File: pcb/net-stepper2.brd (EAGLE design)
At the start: 90.2 x 41.9 mm, 42 parts, among them J1 MICRO-USB, J2 POWER_JACKPTH_LOCK, J3 ENCODER, J4 ENDSTOP2, J5 ENDSTOP1, J6 STEPER, Q1 600mA/40V, Q2 600mA/40V, U1 L6470, U2 CP2104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

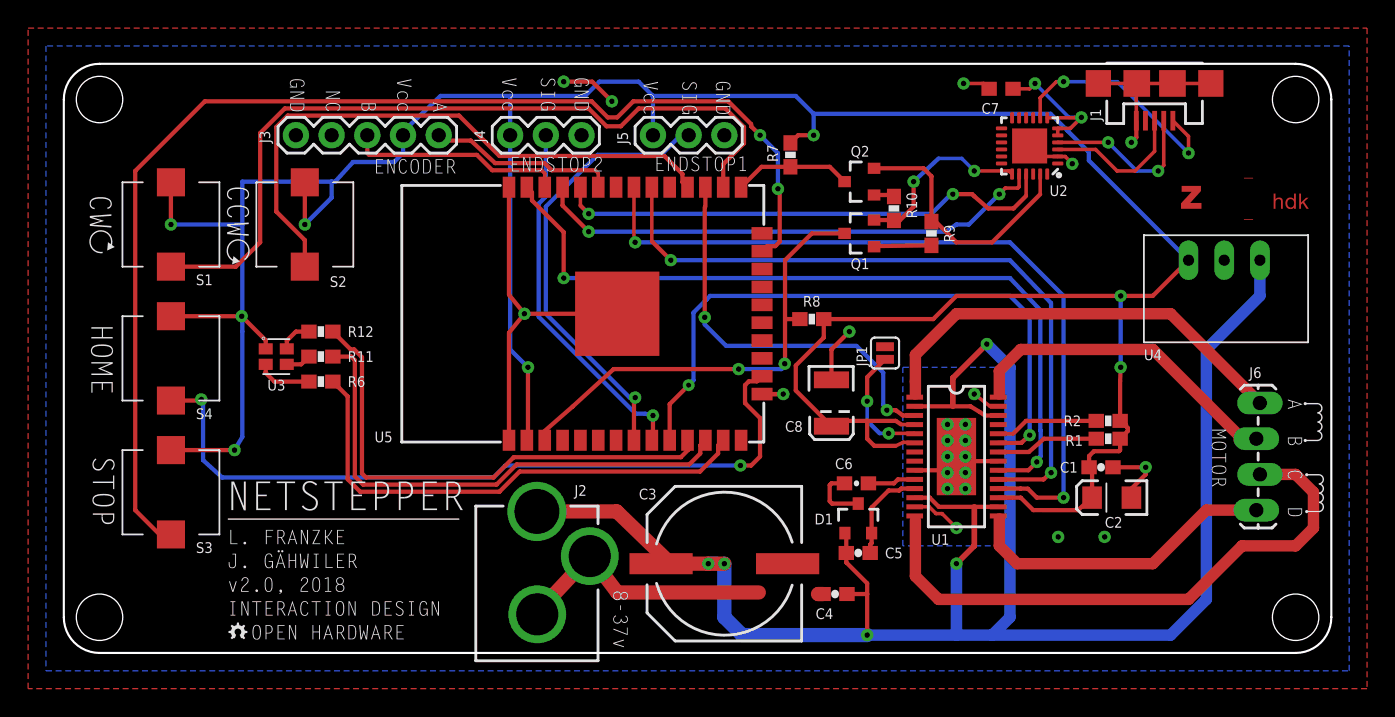
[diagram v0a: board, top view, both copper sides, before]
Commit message: Drill size change
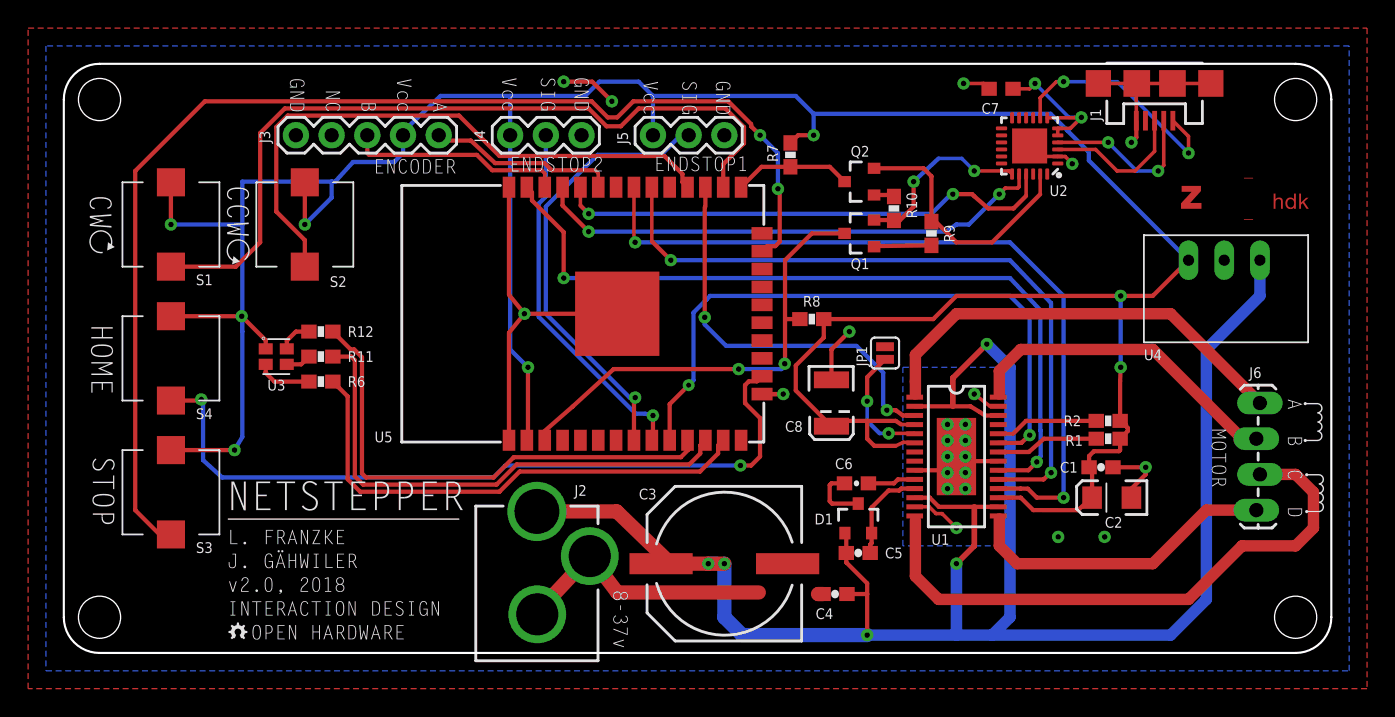
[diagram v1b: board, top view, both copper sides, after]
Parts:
- removed U$10, U$11, U$12, U$9: (no value), RP400N501A:STAND-OFF
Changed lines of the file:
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@@
 <drawing>
 <settings>
-<setting alwaysvectorfont="yes"/>
+<setting alwaysvectorfont="no"/>
 <setting keepoldvectorfont="yes"/>
 <setting verticaltext="up"/>
@@
 <text x="14.478" y="18.669" size="0.762" layer="25" font="vector" ratio="20">U3</text>
 <text x="76.835" y="20.828" size="0.762" layer="25" font="vector" ratio="20">U4</text>
+<hole x="2.54" y="39.37" drill="2.99999375"/>
+<hole x="2.54" y="2.54" drill="2.99999375"/>
+<hole x="87.63" y="2.54" drill="2.99999375"/>
+<hole x="87.63" y="39.37" drill="2.99999375"/>
 </plain>
 <attributes>
@@
 <attribute name="VALUE" x="18.161" y="23.749" size="0.4064" layer="27" font="vector"/>
 </element>
-<element name="U$9" library="RP400N501A" package="STAND-OFF" value="" x="2.54" y="39.37" rot="R270"/>
-<element name="U$10" library="RP400N501A" package="STAND-OFF" value="" x="2.54" y="2.54" rot="R270"/>
-<element name="U$11" library="RP400N501A" package="STAND-OFF" value="" x="87.63" y="2.54" rot="R270"/>
-<element name="U$12" library="RP400N501A" package="STAND-OFF" value="" x="87.63" y="39.37" rot="R270"/>
 <element name="A2" library="IAD_GRAPHIC" package="INTERFACE_NETSTEPPER" value="INTERFACE_NETSTEPPER" x="2.54" y="39.37" rot="R270"/>
 <element name="A1" library="IAD_GRAPHIC" package="ZHDK_LOGO" value="ZHDK_LOGO_METAL" x="78.74" y="33.782"/>
